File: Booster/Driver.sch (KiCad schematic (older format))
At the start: 4 parts, among them IC401 SN754410, U401 74LS86

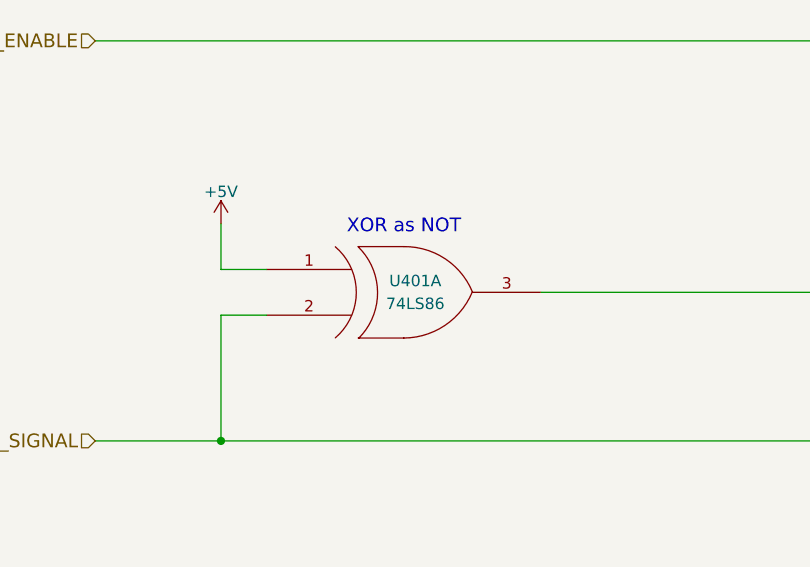
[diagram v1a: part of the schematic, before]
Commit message: Various adjustments based on breadboard prototype.
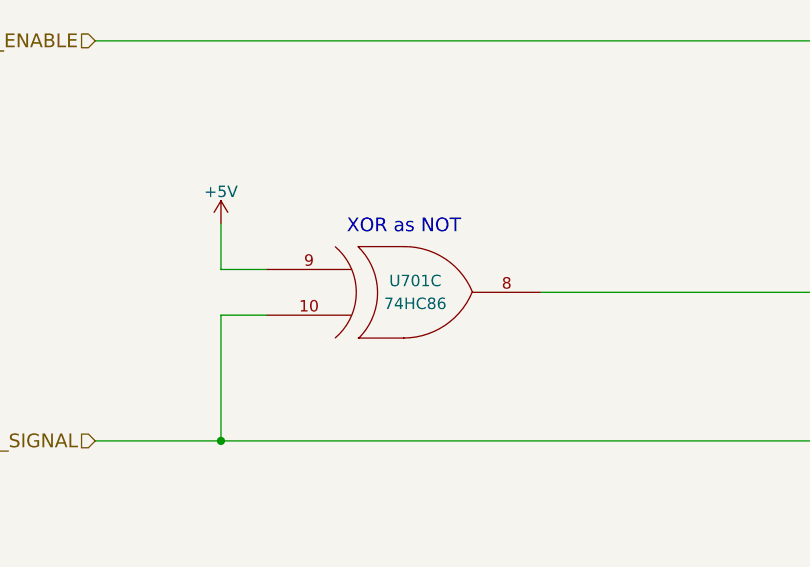
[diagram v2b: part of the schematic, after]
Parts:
- U701: renamed from U401; value 74LS86 -> 74HC86
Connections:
- net +5V: now also U701.9 (IN1); no longer U701.1 (IN1)
- net DRIVER_SIGNAL: now also U701.10 (IN2); no longer U701.2 (IN2)
- net at IC401.15 (SIG2A), IC401.2 (SIG1A): now also U701.8 (OUT); no longer U701.3 (OUT)
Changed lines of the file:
@@
 $EndComp
 $Comp
-L GND #PWR403
+L GND #PWR014
 U 1 1 59E90E44
 P 6950 2900
-F 0 "#PWR403" H 6950 2650 50  0001 C CNN
+F 0 "#PWR014" H 6950 2650 50  0001 C CNN
 F 1 "GND" H 6950 2750 50  0000 C CNN
 F 2 "" H 6950 2900 50  0001 C CNN
@@
 $EndComp
 $Comp
-L GND #PWR405
+L GND #PWR015
 U 1 1 59E90E51
 P 7650 2900
-F 0 "#PWR405" H 7650 2650 50  0001 C CNN
+F 0 "#PWR015" H 7650 2650 50  0001 C CNN
 F 1 "GND" H 7650 2750 50  0000 C CNN
 F 2 "" H 7650 2900 50  0001 C CNN
@@
 Connection ~ 7250 4900
 $Comp
-L GND #PWR404
+L GND #PWR016
 U 1 1 59E90E77
 P 7200 5150
-F 0 "#PWR404" H 7200 4900 50  0001 C CNN
+F 0 "#PWR016" H 7200 4900 50  0001 C CNN
 F 1 "GND" H 7200 5000 50  0000 C CNN
 F 2 "" H 7200 5150 50  0001 C CNN
@@
 $EndComp
 $Comp
-L +5V #PWR402
+L +5V #PWR017
 U 1 1 59E90F12
 P 6950 1800
-F 0 "#PWR402" H 6950 1650 50  0001 C CNN
+F 0 "#PWR017" H 6950 1650 50  0001 C CNN
 F 1 "+5V" H 6950 1940 50  0000 C CNN
 F 2 "" H 6950 1800 50  0001 C CNN
@@
 Connection ~ 8100 6050
 $Comp
-L 74LS86 U401
-U 1 1 5A0F63C2
+L 74LS86 U701
+U 3 1 5A0F63C2
 P 3800 4850
-F 0 "U401" H 3850 4900 50  0000 C CNN
-F 1 "74LS86" H 3850 4800 50  0000 C CNN
+F 0 "U701" H 3850 4900 50  0000 C CNN
+F 1 "74HC86" H 3850 4800 50  0000 C CNN
 F 2 "" H 3800 4850 50  0001 C CNN
 F 3 "" H 3800 4850 50  0001 C CNN
-	1    3800 4850
+	3    3800 4850
 	1    0    0    -1
 $EndComp
@@
 	3000 4750 3000 4550
 $Comp
-L +5V #PWR401
+L +5V #PWR018
 U 1 1 5A0F6545
 P 3000 4550
-F 0 "#PWR401" H 3000 4400 50  0001 C CNN
+F 0 "#PWR018" H 3000 4400 50  0001 C CNN
 F 1 "+5V" H 3000 4690 50  0000 C CNN
 F 2 "" H 3000 4550 50  0001 C CNN

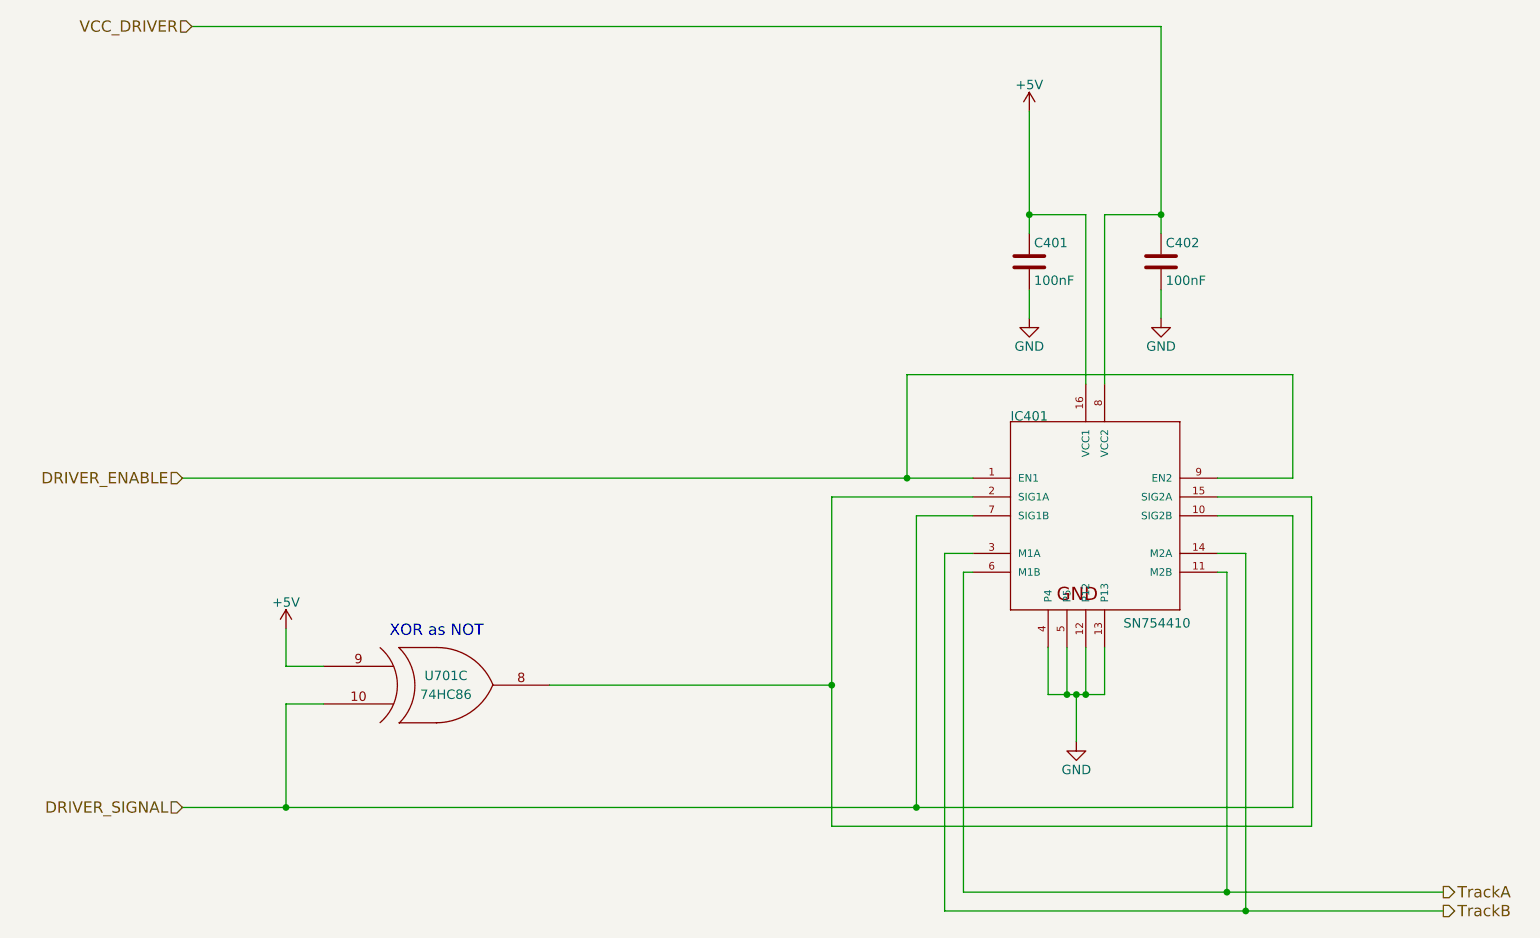
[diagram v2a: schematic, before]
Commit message: Changed to SMD components. Train is now moving. :)
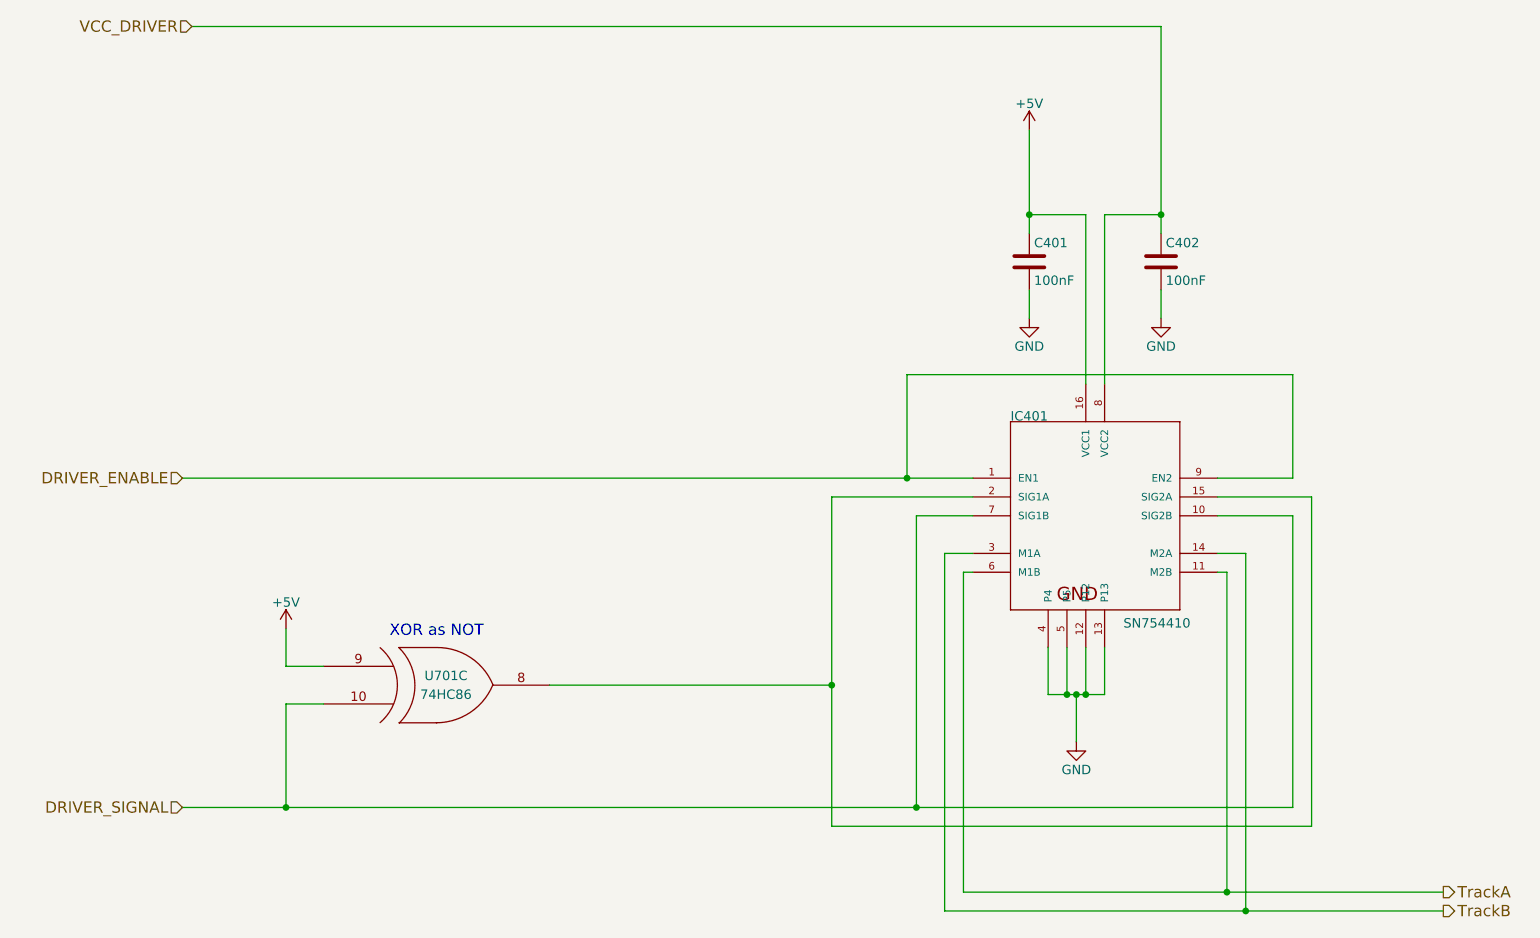
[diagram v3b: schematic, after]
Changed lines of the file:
@@
 $EndComp
 Wire Wire Line
-	6950 1800 6950 2450
+	6950 1900 6950 2350
+Wire Wire Line
+	6950 2350 6950 2450
 Connection ~ 6950 2350
 Wire Wire Line
@@
 	7650 2900 7650 2750
 Wire Wire Line
-	7650 1350 7650 2450
+	7650 1350 7650 2350
+Wire Wire Line
+	7650 2350 7650 2450
 Wire Wire Line
 	7650 2350 7350 2350
 Wire Wire Line
-	5900 3850 5900 5600
+	5900 3850 5900 4850
+Wire Wire Line
+	5900 4850 5900 5600
 Wire Wire Line
 	5900 3850 6650 3850
@@
 	6650 3950 6350 3950
 Wire Wire Line
-	2450 3750 6650 3750
+	2450 3750 6300 3750
+Wire Wire Line
+	6300 3750 6650 3750
 Wire Wire Line
 	7050 4650 7050 4900
 Wire Wire Line
-	7050 4900 7350 4900
+	7050 4900 7150 4900
+Wire Wire Line
+	7150 4900 7200 4900
+Wire Wire Line
+	7200 4900 7250 4900
+Wire Wire Line
+	7250 4900 7350 4900
 Wire Wire Line
 	7200 4900 7200 5150
@@
 L +5V #PWR017
 U 1 1 59E90F12
-P 6950 1800
-F 0 "#PWR017" H 6950 1650 50  0001 C CNN
-F 1 "+5V" H 6950 1940 50  0000 C CNN
-F 2 "" H 6950 1800 50  0001 C CNN
-F 3 "" H 6950 1800 50  0001 C CNN
-	1    6950 1800
+P 6950 1900
+F 0 "#PWR017" H 6950 1750 50  0001 C CNN
+F 1 "+5V" H 6950 2040 50  0000 C CNN
+F 2 "" H 6950 1900 50  0001 C CNN
+F 3 "" H 6950 1900 50  0001 C CNN
+	1    6950 1900
 	1    0    0    -1
 $EndComp
@@
 	6600 4250 6600 5950
 Wire Wire Line
-	6600 5950 9150 5950
+	6600 5950 8000 5950
+Wire Wire Line
+	8000 5950 9150 5950
 Wire Wire Line
 	6650 4150 6500 4150
@@
 	6500 4150 6500 6050
 Wire Wire Line
-	6500 6050 9150 6050
+	6500 6050 8100 6050
+Wire Wire Line
+	8100 6050 9150 6050
 Text HLabel 9150 5950 2    60   Output ~ 0
 TrackA
@@
 	7650 1350 2500 1350
 Wire Wire Line
-	2450 5500 8350 5500
+	2450 5500 3000 5500
+Wire Wire Line
+	3000 5500 6350 5500
+Wire Wire Line
+	6350 5500 8350 5500
 Wire Wire Line
 	8350 5500 8350 3950

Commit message: Annotation, fix missing connection.
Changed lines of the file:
@@
 $EndComp
 Wire Wire Line
-	6950 1900 6950 2350
-Wire Wire Line
-	6950 2350 6950 2450
+	6950 1900 6950 2450
 Connection ~ 6950 2350
 Wire Wire Line
@@
 	7650 2900 7650 2750
 Wire Wire Line
-	7650 1350 7650 2350
-Wire Wire Line
-	7650 2350 7650 2450
+	7650 1350 7650 2450
 Wire Wire Line
 	7650 2350 7350 2350
 Wire Wire Line
-	5900 3850 5900 4850
-Wire Wire Line
-	5900 4850 5900 5600
+	5900 3850 5900 5600
 Wire Wire Line
 	5900 3850 6650 3850
@@
 	6650 3950 6350 3950
 Wire Wire Line
-	2450 3750 6300 3750
-Wire Wire Line
-	6300 3750 6650 3750
+	2450 3750 6650 3750
 Wire Wire Line
 	7050 4650 7050 4900
 Wire Wire Line
-	7050 4900 7150 4900
-Wire Wire Line
-	7150 4900 7200 4900
-Wire Wire Line
-	7200 4900 7250 4900
-Wire Wire Line
-	7250 4900 7350 4900
+	7050 4900 7350 4900
 Wire Wire Line
 	7200 4900 7200 5150
@@
 	6600 4250 6600 5950
 Wire Wire Line
-	6600 5950 8000 5950
-Wire Wire Line
-	8000 5950 9150 5950
+	6600 5950 9150 5950
 Wire Wire Line
 	6650 4150 6500 4150
@@
 	6500 4150 6500 6050
 Wire Wire Line
-	6500 6050 8100 6050
-Wire Wire Line
-	8100 6050 9150 6050
+	6500 6050 9150 6050
 Text HLabel 9150 5950 2    60   Output ~ 0
 TrackA
@@
 	7650 1350 2500 1350
 Wire Wire Line
-	2450 5500 3000 5500
-Wire Wire Line
-	3000 5500 6350 5500
-Wire Wire Line
-	6350 5500 8350 5500
+	2450 5500 8350 5500
 Wire Wire Line
 	8350 5500 8350 3950

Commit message: Assigned footprints & minor adjustments.
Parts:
- C401, C402: footprint (none) -> Capacitors_SMD:C_0805
- IC401: footprint HBridge-DIP16 -> Housings_DIP:DIP-16_W7.62mm
- U701: footprint (none) -> SMD_Packages:SOIC-14_N
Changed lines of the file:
@@
 F 0 "IC401" H 6850 4850 50  0000 L BNN
 F 1 "SN754410" H 7450 3750 50  0000 L BNN
-F 2 "HBridge-DIP16" H 7250 4300 50  0001 C CNN
+F 2 "Housings_DIP:DIP-16_W7.62mm" H 7250 4300 50  0001 C CNN
 F 3 "" H 7250 4150 60  0001 C CNN
 	1    7250 4150
@@
 F 0 "C401" H 6975 2700 50  0000 L CNN
 F 1 "100nF" H 6975 2500 50  0000 L CNN
-F 2 "" H 6988 2450 50  0001 C CNN
+F 2 "Capacitors_SMD:C_0805" H 6988 2450 50  0001 C CNN
 F 3 "" H 6950 2600 50  0001 C CNN
 	1    6950 2600
@@
 F 0 "C402" H 7675 2700 50  0000 L CNN
 F 1 "100nF" H 7675 2500 50  0000 L CNN
-F 2 "" H 7688 2450 50  0001 C CNN
+F 2 "Capacitors_SMD:C_0805" H 7688 2450 50  0001 C CNN
 F 3 "" H 7650 2600 50  0001 C CNN
 	1    7650 2600
@@
 F 0 "U701" H 3850 4900 50  0000 C CNN
 F 1 "74HC86" H 3850 4800 50  0000 C CNN
-F 2 "" H 3800 4850 50  0001 C CNN
+F 2 "SMD_Packages:SOIC-14_N" H 3800 4850 50  0001 C CNN
 F 3 "" H 3800 4850 50  0001 C CNN
 	3    3800 4850
